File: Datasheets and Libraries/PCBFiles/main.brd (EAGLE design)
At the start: 160 x 100 mm, 1 part, among them IC1 ATSAMD21E17A-AUT

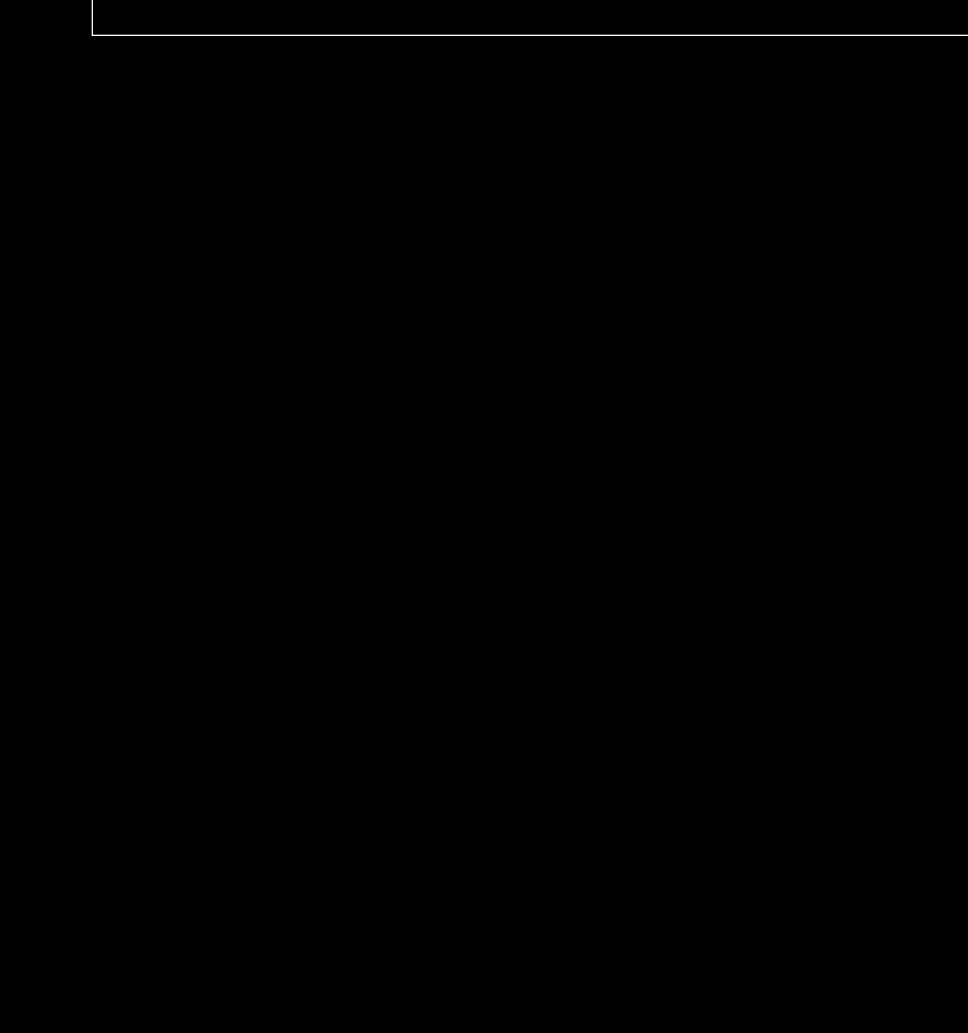
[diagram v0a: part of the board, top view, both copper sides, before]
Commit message: Added Custom Footprint for TEMU ST7735
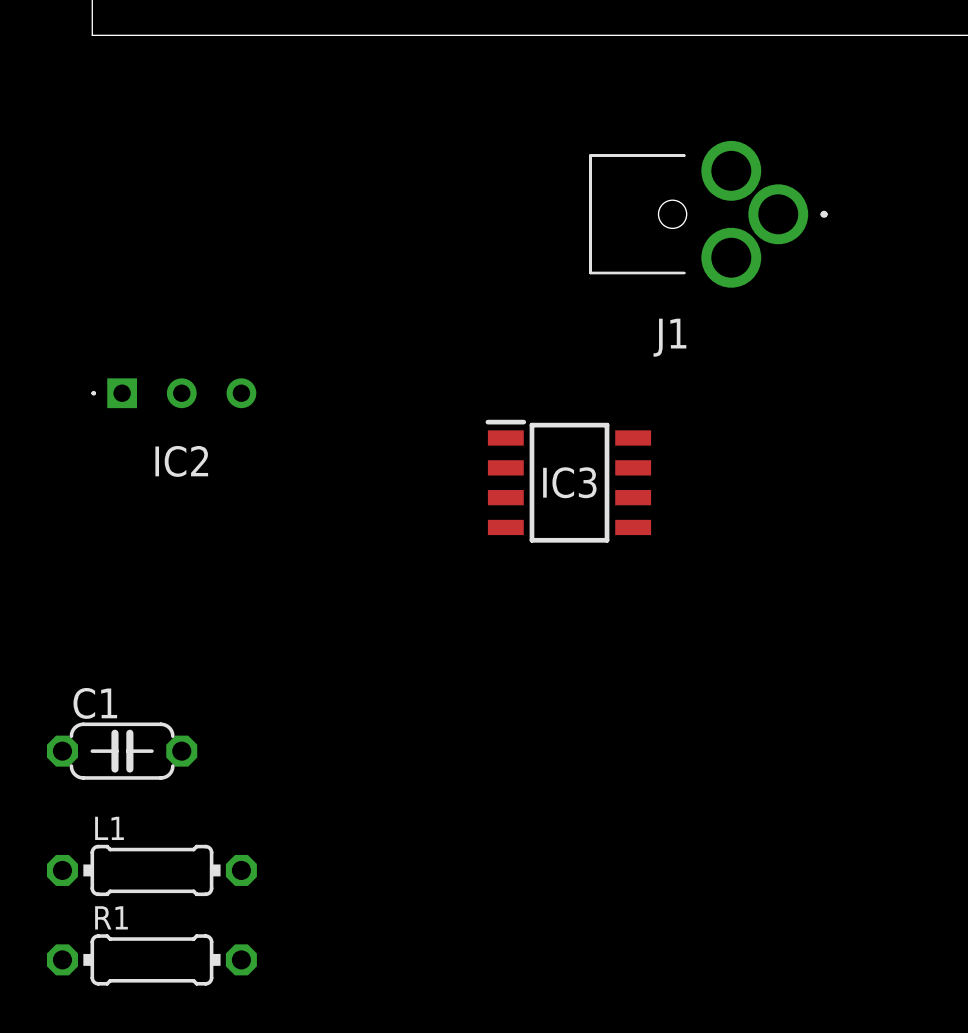
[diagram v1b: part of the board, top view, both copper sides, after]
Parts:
- added C1: (no value), rcl:C050-024X044
- added IC2: AZ431LBZTR-E1, AZ431LBZTR-E1:AZ431LBZTRE1
- added IC3: TPA731D, TPA731D:SOIC127P600X175-8N
- added J1: MJ1-2503A, MJ1-2503A:MJ12503A
- added L1, R1: (no value), rcl:0204/7
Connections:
- new net GND: IC3.7
- new net VDD: IC3.6

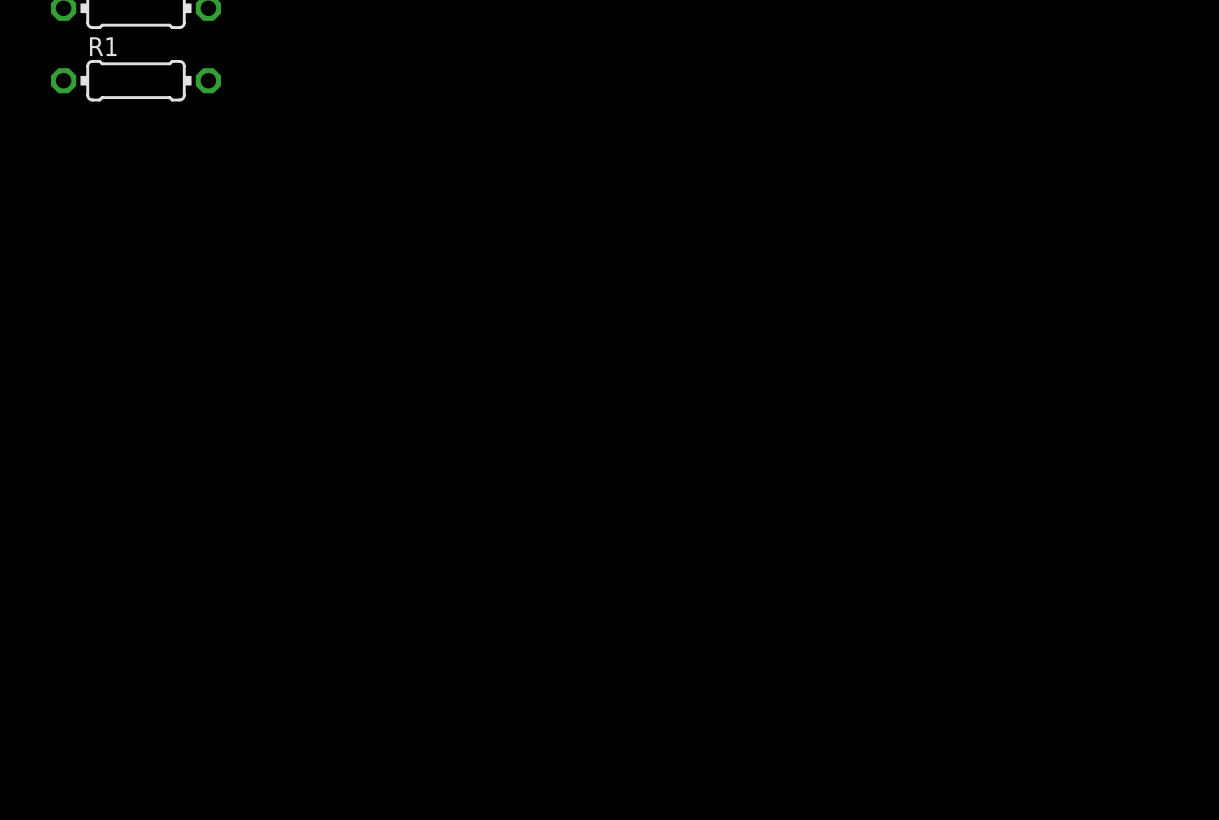
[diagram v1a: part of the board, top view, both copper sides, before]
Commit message: Fixed St7735 footprint
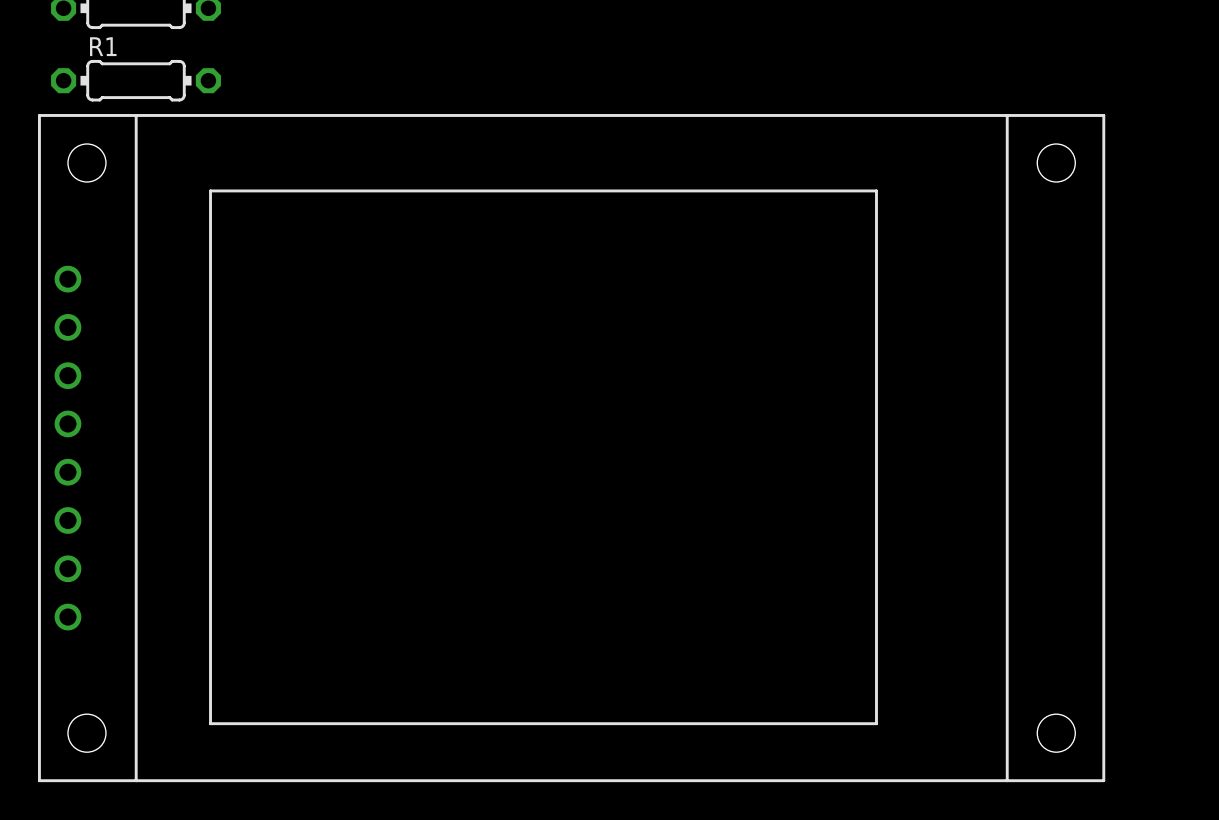
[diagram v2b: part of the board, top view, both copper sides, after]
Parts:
- added U$1: ST7735STEMU, ST7735wosd:ST7735S_NOSD
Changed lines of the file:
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@@
 <attribute name="MOUSER_PRICE-STOCK" value="https://www.mouser.com/Search/Refine.aspx?Keyword=595-TPA731D" x="20.32" y="-19.05" size="1.778" layer="27" display="off"/>
 <attribute name="NAME" x="20.32" y="-19.05" size="1.27" layer="25" align="center"/>
-<attribute name="VALUE" x="20.32" y="-19.05" size="1.27" layer="27" align="center"/>
+<attribute name="VALUE" x="20.32" y="-22.86" size="1.27" layer="27" align="center"/>
 </element>
 <element name="C1" library="rcl" library_urn="urn:adsk.eagle:library:334" package="C050-024X044" package3d_urn="urn:adsk.eagle:package:23643/1" value="" x="1.27" y="-30.48" smashed="yes">
@@
 <attribute name="VALUE" x="0.9144" y="-39.8526" size="0.9906" layer="27" ratio="10"/>
 </element>
+<element name="U$1" library="ST7735wosd" package="ST7735S_NOSD" value="ST7735STEMU" x="-2.54" y="-76.2" smashed="yes"/>
 </elements>
 <signals>
